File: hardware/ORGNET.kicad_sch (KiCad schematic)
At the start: 35 parts, among them J1 Conn_02x08_Odd_Even, SW1 RESET, SW2 BOOTSEL, U1 SN74LVC8T245, U2 SN74LVC8T245, U3 AP2112K-3.3, U4 RP2350A, U5 W25Q128JVP, U6 Raspberry Pi Radio Module 2, Y1 12M

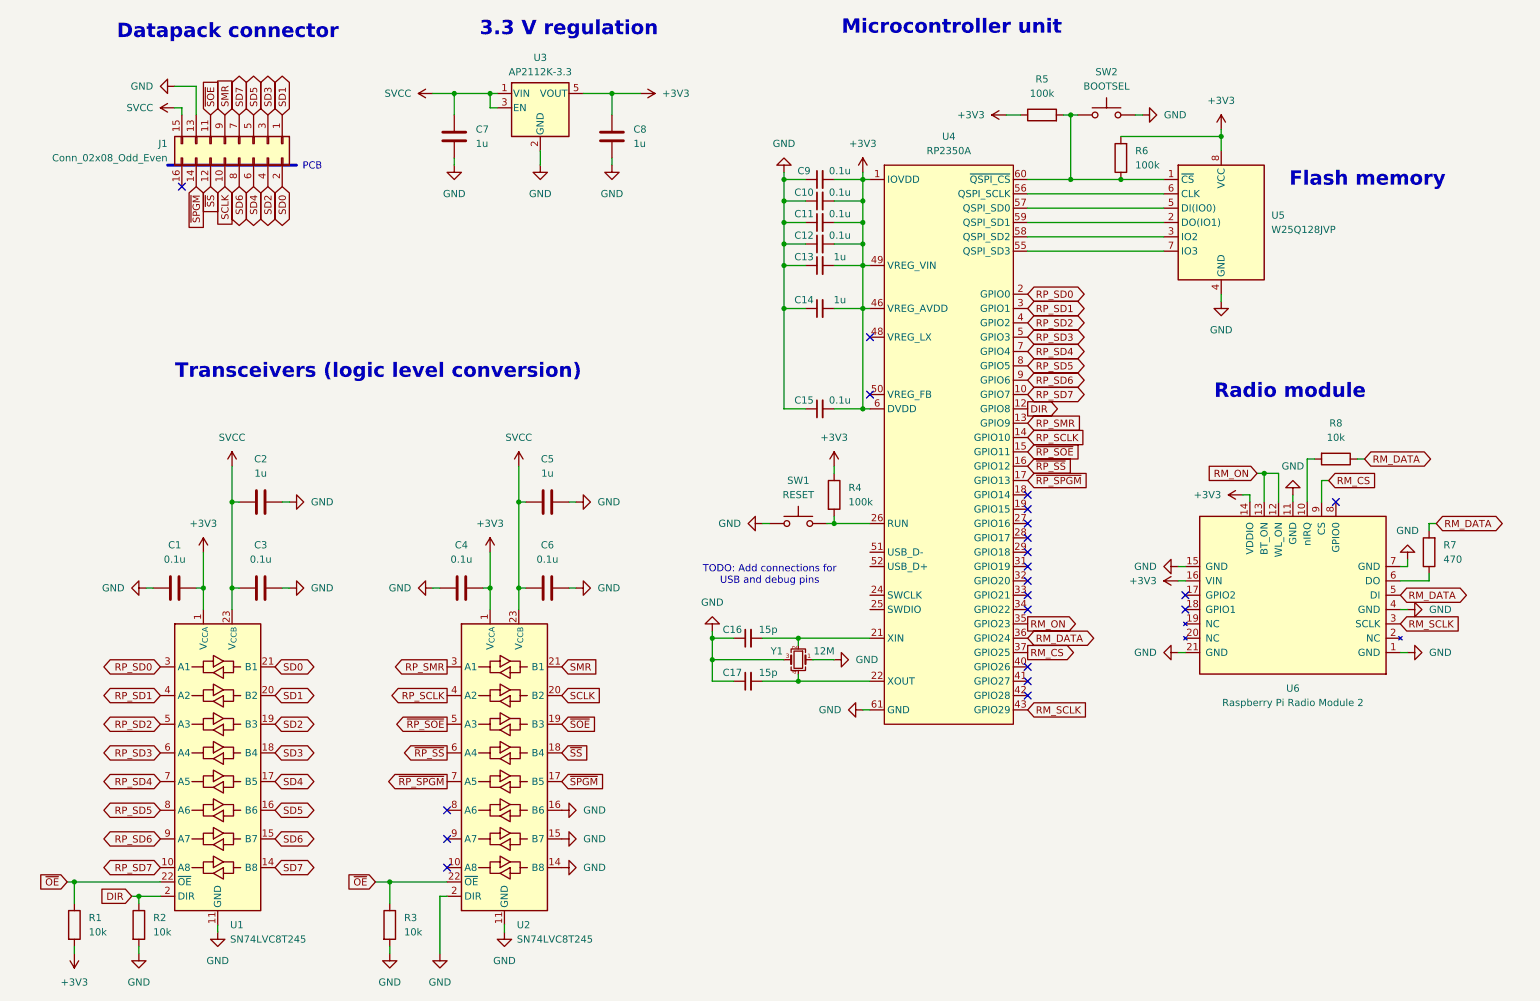
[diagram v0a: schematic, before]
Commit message: Add expansion and debug headers
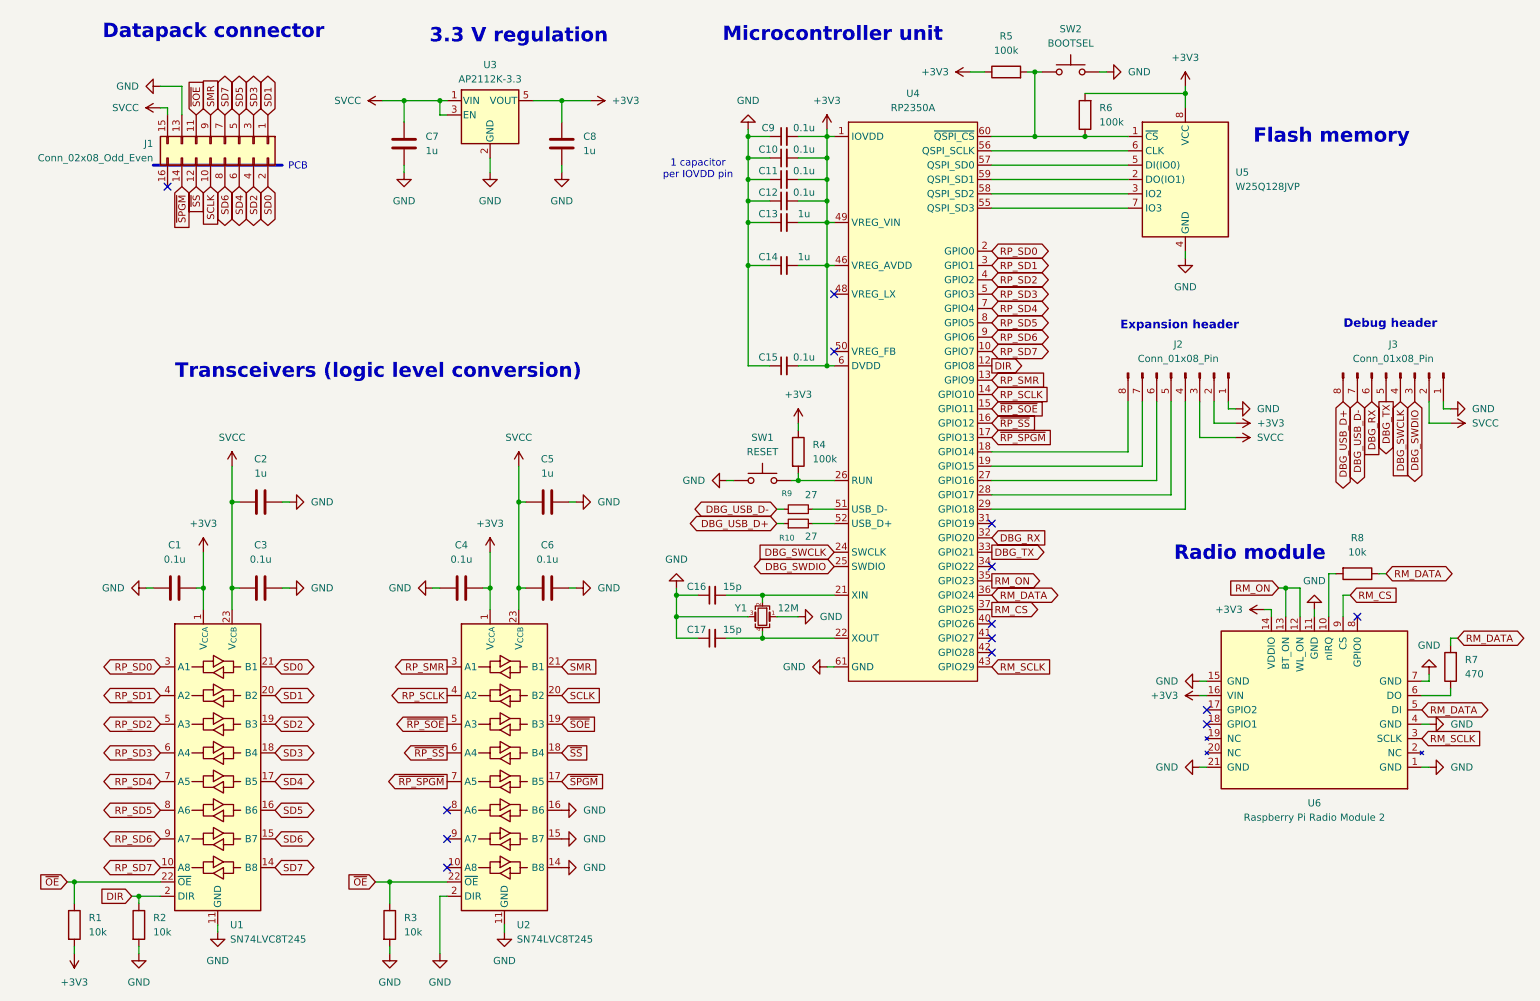
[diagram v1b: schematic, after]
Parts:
- added J2, J3: Conn_01x08_Pin, symbol Connector:Conn_01x08_Pin
- added R10, R9: 27, symbol Device:R_Small
- U4: footprint Package_DFN_QFN_Extra:QFN-60_EP_7x7_Pitch0.4mm -> (none)
- U6: footprint (none) -> RP-RM2:rpi_rmc20452t
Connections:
- net +3V3: now also J2.2 (Pin_2)
- net GND: now also J2.1 (Pin_1), J3.1 (Pin_1)
- net SVCC: now also J2.3 (Pin_3), J3.2 (Pin_2)
- net at U4.18 (GPIO14): now also J2.8 (Pin_8)
- net at U4.19 (GPIO15): now also J2.7 (Pin_7)
- net DBG_SWCLK: now reaches U4.24 (SWCLK)
- net DBG_SWCLK: now also J3.4 (Pin_4)
- net DBG_SWDIO: now reaches U4.25 (SWDIO)
- net DBG_SWDIO: now also J3.3 (Pin_3)
- net at U4.27 (GPIO16): now also J2.6 (Pin_6)
- net at U4.28 (GPIO17): now also J2.5 (Pin_5)
- net at U4.29 (GPIO18): now also J2.4 (Pin_4)
- net DBG_RX: now reaches U4.32 (GPIO20)
- net DBG_RX: now also J3.6 (Pin_6)
- net DBG_TX: now reaches U4.33 (GPIO21)
- net DBG_TX: now also J3.5 (Pin_5)
- net at U4.51 (USB_D-): now also R9.2
- net at U4.52 (USB_D+): now also R10.2
- new net DBG_USB_D+: J3.8 (Pin_8), R10.1
- new net DBG_USB_D-: J3.7 (Pin_7), R9.1
- no-connect marks 21 -> 14
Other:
- note added: "1 capacitor per IOVDD pin"
- note added: "Debug header"
- note added: "Expansion header"
- note removed: "TODO: Add connections for USB and debug pins"
- moved on the sheet: C10, C11, C12, C13, C14, C15, C16, C17, C7, C8, C9, J1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

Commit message: Begin laying out footprints on PCB
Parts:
- removed J2, J3: Conn_01x08_Pin, symbol Connector:Conn_01x08_Pin
- removed R10, R9: 27, symbol Device:R_Small
- removed SW1: RESET, symbol Switch:SW_Push
- removed SW2: BOOTSEL, symbol Switch:SW_Push
- added C14, C15: 1u, Capacitor_SMD:C_0201_0603Metric_Pad0.64x0.40mm_HandSolder, symbol Device:C_Small
- added J3: Conn_01x03, Connector_JST:JST_SH_BM03B-SRSS-TB_1x03-1MP_P1.00mm_Vertical, symbol Connector_Generic:Conn_01x03
- added TP1, TP2, TP3: TestPoint, TestPoint:TestPoint_Pad_D2.0mm, symbol Connector:TestPoint
- added TP4: RESET, TestPoint:TestPoint_Pad_D2.0mm, symbol Connector:TestPoint
- added TP5: BOOTSEL, TestPoint:TestPoint_Pad_D2.0mm, symbol Connector:TestPoint
- C1, C10, C11, C12, C13, C2, C3, C4, C5, C6, C7, C8, C9: footprint (none) -> Capacitor_SMD:C_0201_0603Metric_Pad0.64x0.40mm_HandSolder
- C16: renamed from C14; footprint (none) -> Capacitor_SMD:C_0201_0603Metric_Pad0.64x0.40mm_HandSolder
- C17: renamed from C15; footprint (none) -> Capacitor_SMD:C_0201_0603Metric_Pad0.64x0.40mm_HandSolder
- C18: renamed from C16; footprint (none) -> Capacitor_SMD:C_0201_0603Metric_Pad0.64x0.40mm_HandSolder
- C19: renamed from C17; footprint (none) -> Capacitor_SMD:C_0201_0603Metric_Pad0.64x0.40mm_HandSolder
- J1: footprint (none) -> Connector_PinSocket_2.54mm:PinSocket_2x08_P2.54mm_Horizontal
- R1, R2, R3, R4, R5, R6, R7, R8: footprint (none) -> Resistor_SMD:R_0201_0603Metric_Pad0.64x0.40mm_HandSolder
- U1, U2: footprint (none) -> Package_SO:TSSOP-24_4.4x7.8mm_P0.65mm
- U4: footprint (none) -> Package_DFN_QFN:QFN-60-1EP_7x7mm_P0.4mm_EP3.4x3.4mm
- Y1: footprint (none) -> Crystal:Crystal_SMD_Abracon_ABM8G-4Pin_3.2x2.5mm
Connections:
- net +3V3: now also R3.2, C14.2, C15.2, TP2.1
- net DBG_SWCLK: now also J3.1 (Pin_1)
- net DBG_SWDIO: now also J3.3 (Pin_3)
- net GND: now also C14.1, C15.1, J3.2 (Pin_2), TP1.1; no longer R3.2
- net RP_SCLK: now also U2.6 (A4); no longer U2.4 (A2)
- net RP_SD0: now also U1.10 (A8); no longer U1.3 (A1)
- net RP_SD1: now also U1.9 (A7); no longer U1.4 (A2)
- net RP_SD2: now also U1.8 (A6); no longer U1.5 (A3)
- net RP_SD3: now also U1.7 (A5); no longer U1.6 (A4)
- net RP_SD4: now also U1.6 (A4); no longer U1.7 (A5)
- net RP_SD5: now also U1.5 (A3); no longer U1.8 (A6)
- net RP_SD6: now also U1.4 (A2); no longer U1.9 (A7)
- net RP_SD7: now also U1.3 (A1); no longer U1.10 (A8)
- net RP_SMR: now also U2.7 (A5); no longer U2.3 (A1)
- net SCLK: now also U2.18 (B4); no longer U2.20 (B2)
- net SD0: now also U1.14 (B8); no longer U1.21 (B1)
- net SD1: now also U1.15 (B7); no longer U1.20 (B2)
- net SD2: now also U1.16 (B6); no longer U1.19 (B3)
- net SD3: now also U1.17 (B5); no longer U1.18 (B4)
- net SD4: now also U1.18 (B4); no longer U1.17 (B5)
- net SD5: now also U1.19 (B3); no longer U1.16 (B6)
- net SD6: now also U1.20 (B2); no longer U1.15 (B7)
- net SD7: now also U1.21 (B1); no longer U1.14 (B8)
- net SMR: now also U2.17 (B5); no longer U2.21 (B1)
- net SVCC: now also TP3.1
- net ~{RP_SPGM}: now also U2.3 (A1); no longer U2.7 (A5)
- net ~{RP_SS}: now also U2.4 (A2); no longer U2.6 (A4)
- net ~{SPGM}: now also U2.21 (B1); no longer U2.17 (B5)
- net ~{SS}: now also U2.20 (B2); no longer U2.18 (B4)
- net at R4.2, U4.26 (RUN): now also TP4.1
- net at R5.2, R6.1, U4.60 (~{QSPI_CS})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: now also TP5.1
- net DBG_RX: no longer names the net of U4.32 (GPIO20)
- net DBG_TX: no longer names the net of U4.33 (GPIO21)
- no-connect marks 14 -> 23
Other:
- note removed: "Expansion header"
- moved on the sheet: C10, C11, C12, C13, C9

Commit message: Start routing PCB
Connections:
- net GND: now also U2.19 (B3), U2.20 (B2), U2.21 (B1); no longer U2.14 (B8), U2.15 (B7), U2.16 (B6)
- net RP_SCLK: now also U2.9 (A7); no longer U2.6 (A4)
- net RP_SMR: now also U2.10 (A8); no longer U2.7 (A5)
- net SCLK: now also U2.15 (B7); no longer U2.18 (B4)
- net SMR: now also U2.14 (B8); no longer U2.17 (B5)
- net ~{RP_SOE}: now also U2.8 (A6); no longer U2.5 (A3)
- net ~{RP_SPGM}: now also U2.6 (A4); no longer U2.3 (A1)
- net ~{RP_SS}: now also U2.7 (A5); no longer U2.4 (A2)
- net ~{SOE}: now also U2.16 (B6); no longer U2.19 (B3)
- net ~{SPGM}: now also U2.18 (B4); no longer U2.21 (B1)
- net ~{SS}: now also U2.17 (B5); no longer U2.20 (B2)

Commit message: Fix order of pins on connector
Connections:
- net DIR: now also U2.2 (DIR), U4.10 (GPIO7); no longer U1.2 (DIR), U4.12 (GPIO8)
- net GND: now also U1.14 (B8), U1.15 (B7), U1.16 (B6), U1.2 (DIR); no longer U2.19 (B3), U2.2 (DIR), U2.20 (B2), U2.21 (B1)
- net RP_SCLK: now also U1.3 (A1), U4.7 (GPIO4); no longer U2.9 (A7), U4.14 (GPIO10)
- net RP_SD0: now also U2.3 (A1), U4.19 (GPIO15); no longer U1.10 (A8), U4.2 (GPIO0)
- net RP_SD1: now also U2.4 (A2), U4.18 (GPIO14); no longer U1.9 (A7), U4.3 (GPIO1)
- net RP_SD2: now also U2.5 (A3), U4.17 (GPIO13); no longer U1.8 (A6), U4.4 (GPIO2)
- net RP_SD3: now also U2.6 (A4), U4.16 (GPIO12); no longer U1.7 (A5), U4.5 (GPIO3)
- net RP_SD4: now also U2.7 (A5), U4.15 (GPIO11); no longer U1.6 (A4), U4.7 (GPIO4)
- net RP_SD5: now also U2.8 (A6), U4.14 (GPIO10); no longer U1.5 (A3), U4.8 (GPIO5)
- net RP_SD6: now also U2.9 (A7), U4.13 (GPIO9); no longer U1.4 (A2), U4.9 (GPIO6)
- net RP_SD7: now also U2.10 (A8), U4.12 (GPIO8); no longer U1.3 (A1), U4.10 (GPIO7)
- net RP_SMR: now also U1.4 (A2), U4.5 (GPIO3); no longer U2.10 (A8), U4.13 (GPIO9)
- net SCLK: now also U1.21 (B1); no longer U2.15 (B7)
- net SD0: now also U2.21 (B1); no longer U1.14 (B8)
- net SD1: now also U2.20 (B2); no longer U1.15 (B7)
- net SD2: now also U2.19 (B3); no longer U1.16 (B6)
- net SD3: now also U2.18 (B4); no longer U1.17 (B5)
- net SD4: now also U2.17 (B5); no longer U1.18 (B4)
- net SD5: now also U2.16 (B6); no longer U1.19 (B3)
- net SD6: now also U2.15 (B7); no longer U1.20 (B2)
- net SD7: now also U2.14 (B8); no longer U1.21 (B1)
- net SMR: now also U1.20 (B2); no longer U2.14 (B8)
- net ~{RP_SOE}: now also U1.6 (A4), U4.3 (GPIO1); no longer U2.8 (A6), U4.15 (GPIO11)
- net ~{RP_SPGM}: now also U1.7 (A5), U4.2 (GPIO0); no longer U2.6 (A4), U4.17 (GPIO13)
- net ~{RP_SS}: now also U1.5 (A3), U4.4 (GPIO2); no longer U2.7 (A5), U4.16 (GPIO12)
- net ~{SOE}: now also U1.18 (B4); no longer U2.16 (B6)
- net ~{SPGM}: now also U1.17 (B5); no longer U2.18 (B4)
- net ~{SS}: now also U1.19 (B3); no longer U2.17 (B5)
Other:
- moved on the sheet: R1, R2, R3

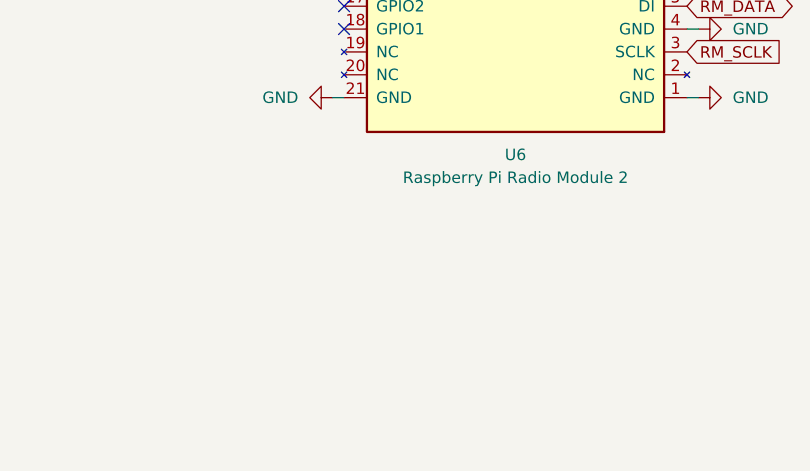
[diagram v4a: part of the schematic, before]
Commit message: Add branding to schematics
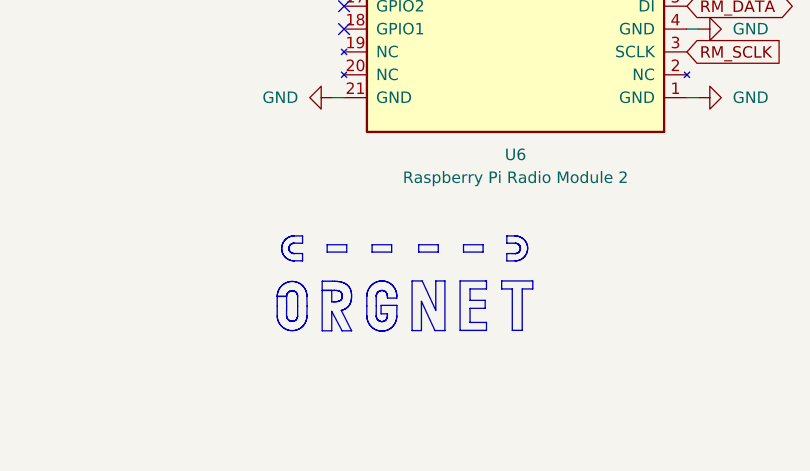
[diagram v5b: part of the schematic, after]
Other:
- company: (none) -> James Livesey
- title: (none) -> ORGNET
